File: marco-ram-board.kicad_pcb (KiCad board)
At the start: 4 copper layers, 160 x 100 mm, 185 parts, among them J201 PRG_USB, J202 MCU_RST, J203 MCU_BOOT0, J204 FT_TXD, J205 FT_RXD, J206 CONN_JTAG, J301 CONN_MCU_SERIAL, J302 CONN_EXT, J501 MCU_USB, J502 SD_Card, J503 CONN_DISP, J504 RJ45_Amphenol_RJMG1BD3B8K1ANR, J601 CONN_JACK_12V, J602 CONN_SCREW_12V, Q201 MMBT3906, Q601 DMP3037LSS, SW301 SW_RST, SW302 SW_BOOT0, SW501 BTN0, SW502 BTN1, SW503 BTN2, SW504 BTN3, SW601 PWR_SW, U201 FT2232HL, U301 STM32F765IITx, U401 IS42S86400D, U402 IS42S86400D, U403 IS42S86400D, U404 IS42S86400D, U405 IS42S86400D, U406 IS42S86400D, U407 IS42S86400D, U408 IS42S86400D, U501 KSZ8081RNA, U601 LM2576S-3.3, Y201 12MHz, Y301 25MHz

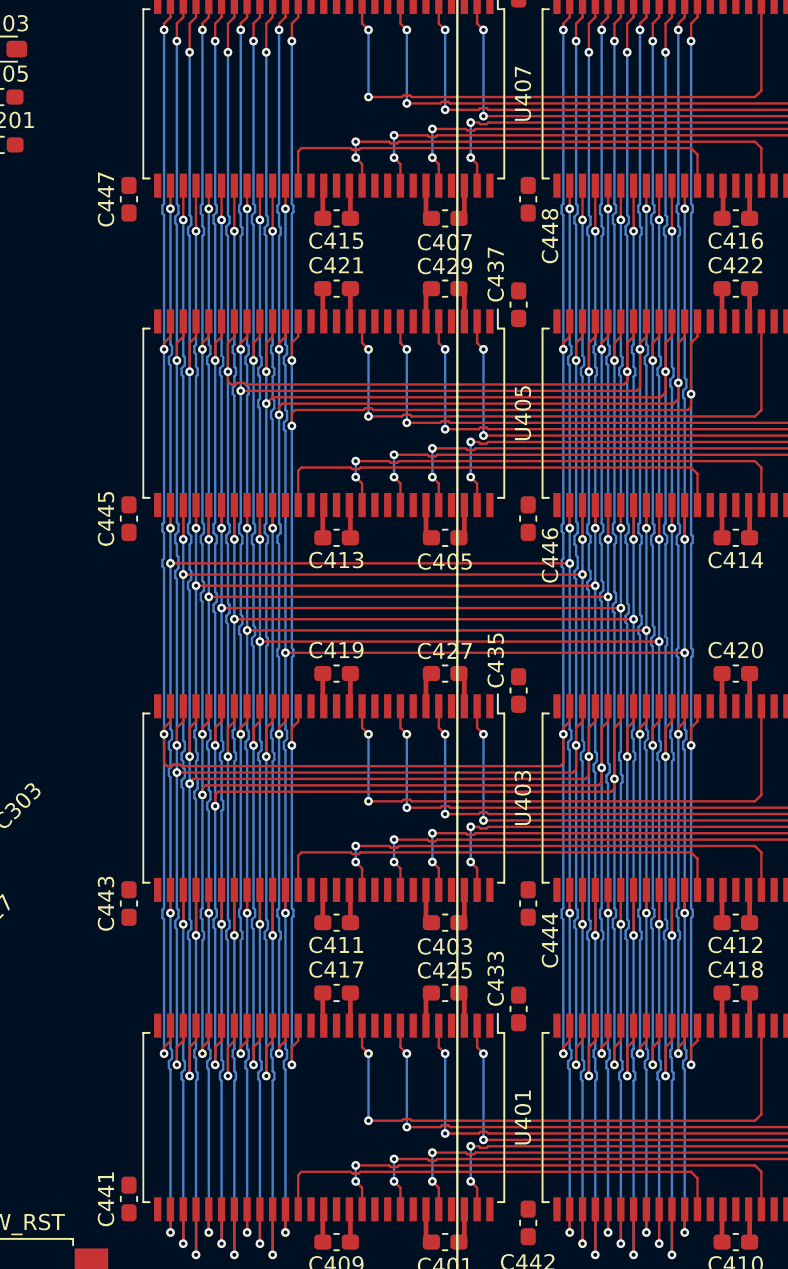
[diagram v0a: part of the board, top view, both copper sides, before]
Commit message: Bring out all SDRAM BUS elements from the SDRAM section from the closest point to the MCU
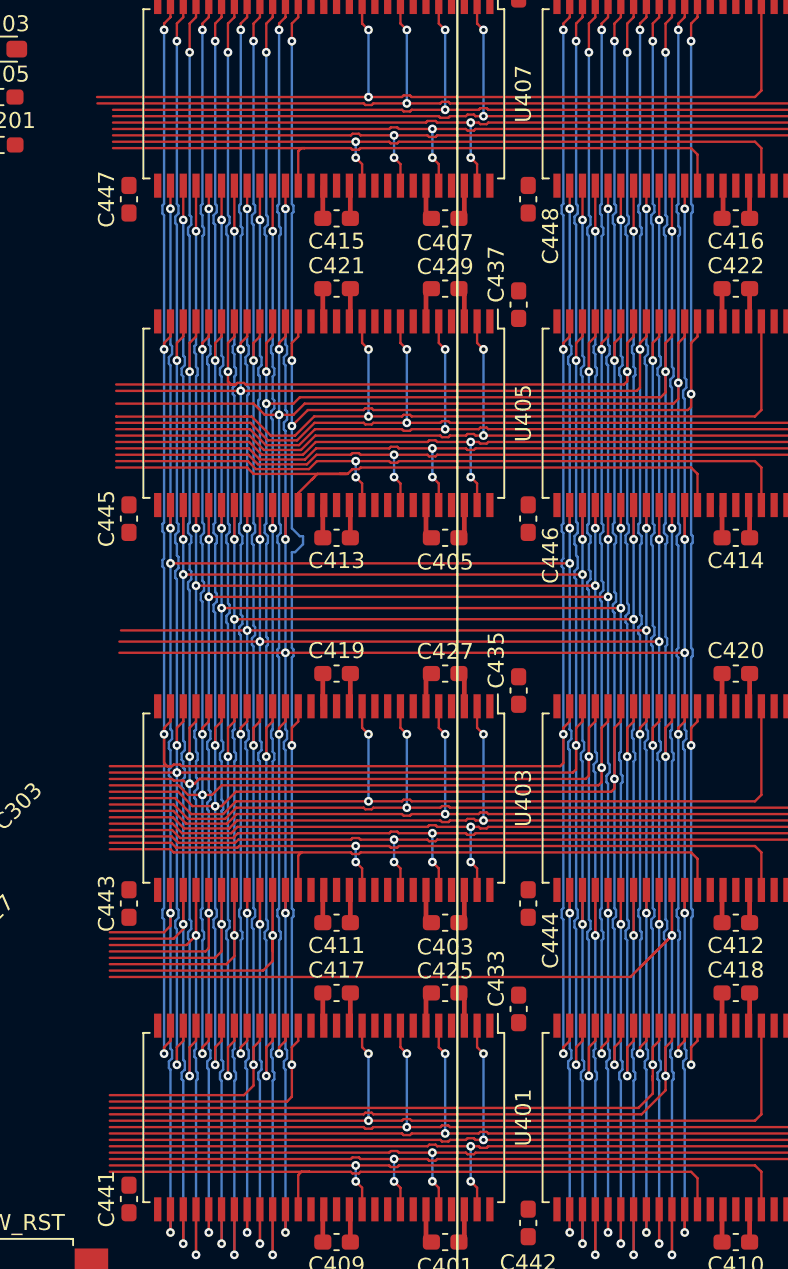
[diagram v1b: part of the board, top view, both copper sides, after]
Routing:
- net /mcu/SDRAM.CKE1: track 74.6 -> 113.7 mm
- net /mcu/SDRAM.~{CS1}: track 75.2 -> 111.7 mm
- net /mcu/SDRAM.~{RAS}: track 182.5 -> 218.9 mm
- net /mcu/SDRAM.D16: track 38.8 -> 62.9 mm
- net /mcu/SDRAM.D8: track 38.8 -> 62.7 mm
- net /mcu/SDRAM.D24: track 38.8 -> 62.4 mm
- net /mcu/SDRAM.D0: track 38.8 -> 62.2 mm
- net /mcu/SDRAM.D23: track 33.3 -> 56.4 mm
- net /mcu/SDRAM.D15: track 33.3 -> 56.3 mm
- net /mcu/SDRAM.D31: track 33.3 -> 56.0 mm
- net /mcu/SDRAM.D7: track 33.3 -> 55.8 mm
- net /mcu/SDRAM.D17: track 38.1 -> 59.8 mm
- net /mcu/SDRAM.D9: track 38.1 -> 59.6 mm
- net /mcu/SDRAM.D25: track 38.1 -> 59.2 mm
- net /mcu/SDRAM.D1: track 38.1 -> 59.0 mm
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
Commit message: Route SDRAM. Whew!
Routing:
- net /mcu/SDRAM.D26: track 56.0 -> 137.8 mm, vias 2 -> 4
- net /mcu/SDRAM.D27: track 52.7 -> 133.7 mm, vias 2 -> 4
- net /mcu/SDRAM.D25: track 59.2 -> 135.9 mm, vias 2 -> 4
- net /mcu/SDRAM.D24: track 62.4 -> 138.6 mm, vias 2 -> 4
- net /mcu/SDRAM.~{BL0}: track 41.4 -> 114.7 mm, vias 0 -> 2
- net /mcu/SDRAM.~{BL3}: track 41.9 -> 109.6 mm, vias 0 -> 2
- net /mcu/SDRAM.D28: track 46.3 -> 113.4 mm, vias 2 -> 4
- net /mcu/SDRAM.D29: track 49.6 -> 116.3 mm, vias 2 -> 4
- net /mcu/SDRAM.D7: track 55.8 -> 120.1 mm, vias 2 -> 4
- net /mcu/SDRAM.D6: track 52.6 -> 115.5 mm, vias 2 -> 4
- net /mcu/SDRAM.D5: track 49.4 -> 111.9 mm, vias 2 -> 4
- net /mcu/SDRAM.D4: track 46.1 -> 108.2 mm, vias 2 -> 4
- net /mcu/SDRAM.D30: track 52.8 -> 113.4 mm
- net /mcu/SDRAM.~{BL1}: track 43.8 -> 104.3 mm, vias 0 -> 2
- net /mcu/SDRAM.D31: track 56.0 -> 115.7 mm
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
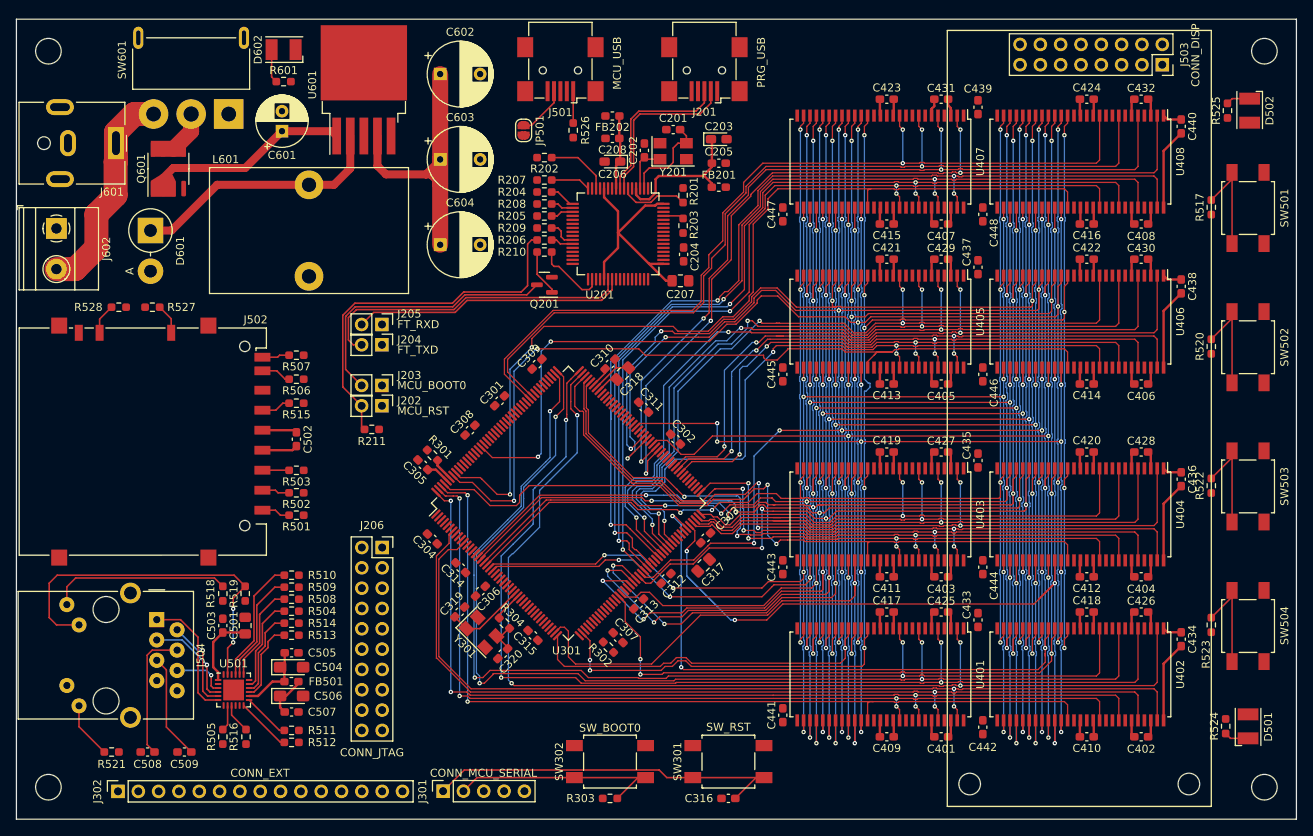
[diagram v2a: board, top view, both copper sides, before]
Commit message: SDRAM routing cleanup
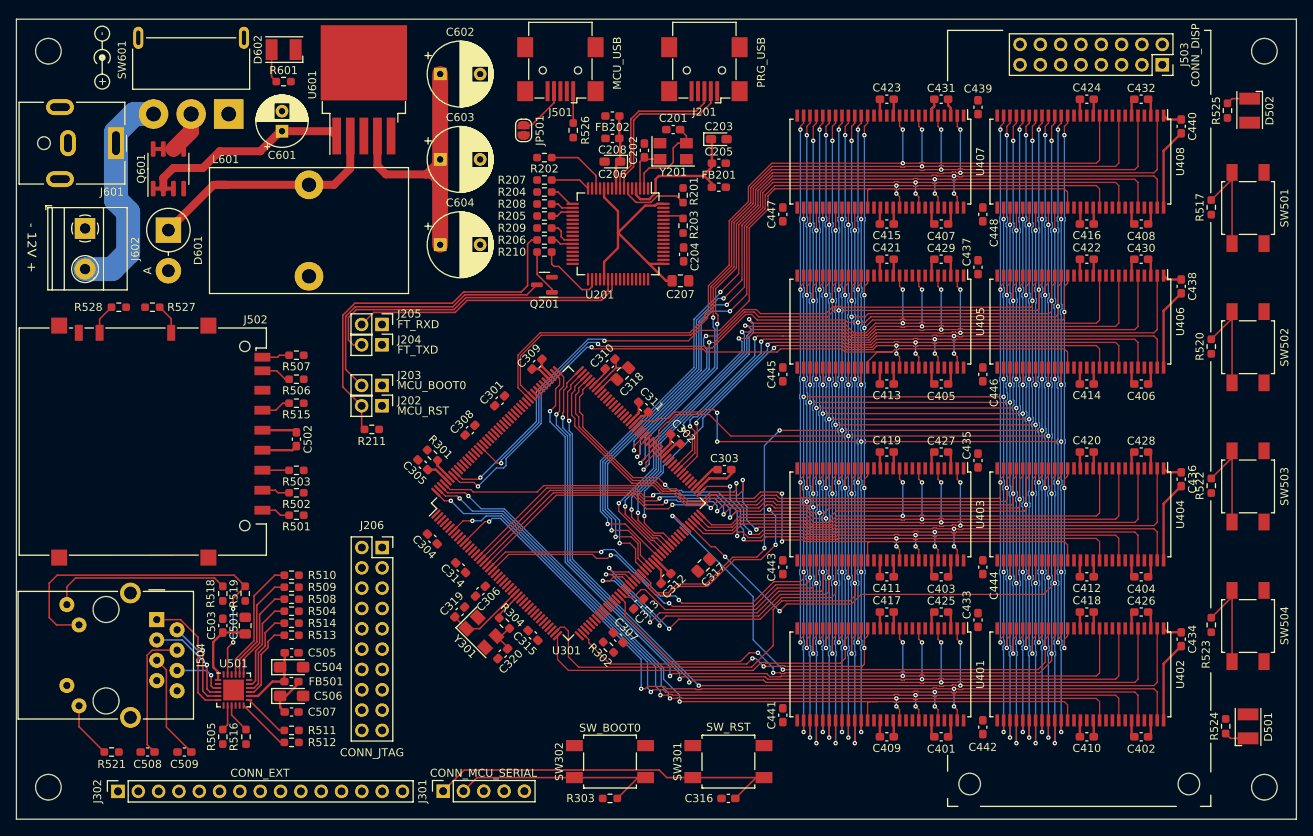
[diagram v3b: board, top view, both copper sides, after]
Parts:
- added REF**: Symbol_Barrel_Polarity, Symbol:Symbol_Barrel_Polarity, F.Cu at (80.8, 44.8)
- moved C303 8.85 mm to (158.5, 96.3), turned to 0 degrees
- moved J602 3.58 mm to (78.6, 66.2)
- moved D601 2.24 mm to (89.0, 66.4)
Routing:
- net /mcu/SDRAM.D26: track 137.8 -> 113.6 mm
- net /mcu/SDRAM.D27: track 133.7 -> 110.7 mm
- net /mcu/SDRAM.D24: track 138.6 -> 118.3 mm
- net /mcu/SDRAM.D25: track 135.9 -> 116.3 mm
- net GND: track 117.9 -> 134.3 mm
- net VDD: track 131.7 -> 146.1 mm
- net /mcu/SDRAM.CKE1: track 140.1 -> 126.1 mm
- net /mcu/SDRAM.~{BL3}: track 109.6 -> 96.3 mm
- net /mcu/SDRAM.D28: track 113.4 -> 100.5 mm
- net /mcu/SDRAM.D29: track 116.3 -> 104.1 mm
- net /mcu/SDRAM.~{BL1}: track 104.3 -> 94.6 mm
- net /mcu/SDRAM.~{BL0}: track 114.7 -> 105.4 mm
- net /mcu/SDRAM.D31: track 115.7 -> 107.0 mm, vias 2 -> 4
- net /mcu/SDRAM.D30: track 113.4 -> 104.8 mm, vias 2 -> 4
- net /mcu/SDRAM.BA0: track 219.6 -> 211.5 mm
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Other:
- board text added: "+"
- board text added: "-"
- board text added: "- 12V +"

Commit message: MCU USB
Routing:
- net /mcu-if/USB.DM: track 0.00 -> 48.9 mm, vias 0 -> 2
- net /mcu-if/USB.ID: track 0.00 -> 48.4 mm, vias 0 -> 2
- net /mcu-if/USB.DP: track 0.00 -> 47.8 mm, vias 0 -> 2
- net /mcu-if/USB.VBUS: track 0.00 -> 44.7 mm, vias 0 -> 2
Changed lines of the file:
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@@
   (segment (start 126.344974 75.15) (end 143.144975 75.15) (width 0.2) (layer "F.Cu") (net 34))
   (segment (start 139.6 49) (end 139.6 52.975) (width 0.2) (layer "F.Cu") (net 57))
+  (segment (start 137.4 53.8) (end 138.35 52.85) (width 0.2) (layer "F.Cu") (net 58))
+  (segment (start 138.35 52.85) (end 138.35 50.95) (width 0.2) (layer "F.Cu") (net 58))
+  (segment (start 138.8 50.5) (end 138.8 49) (width 0.2) (layer "F.Cu") (net 58))
+  (segment (start 138.35 50.95) (end 138.8 50.5) (width 0.2) (layer "F.Cu") (net 58))
+  (segment (start 142.7 88.668272) (end 142.7 89.2) (width 0.2) (layer "F.Cu") (net 58))
+  (segment (start 143.896714 87.471558) (end 142.7 88.668272) (width 0.2) (layer "F.Cu") (net 58))
+  (segment (start 142.7 89.2) (end 142.3 89.6) (width 0.2) (layer "F.Cu") (net 58))
+  (via (at 137.4 53.8) (size 0.55) (drill 0.25) (layers "F.Cu" "B.Cu") (net 58))
+  (via (at 142.3 89.6) (size 0.55) (drill 0.25) (layers "F.Cu" "B.Cu") (net 58))
+  (segment (start 145.75 85.45) (end 142.7 88.5) (width 0.2) (layer "B.Cu") (net 58))
+  (segment (start 138.35 54.75) (end 138.35 69.255026) (width 0.2) (layer "B.Cu") (net 58))
+  (segment (start 138.35 69.255026) (end 145.75 76.655026) (width 0.2) (layer "B.Cu") (net 58))
+  (segment (start 142.7 89.2) (end 142.3 89.6) (width 0.2) (layer "B.Cu") (net 58))
+  (segment (start 145.75 76.655026) (end 145.75 85.45) (width 0.2) (layer "B.Cu") (net 58))
+  (segment (start 142.7 88.5) (end 142.7 89.2) (width 0.2) (layer "B.Cu") (net 58))
+  (segment (start 137.4 53.8) (end 138.35 54.75) (width 0.2) (layer "B.Cu") (net 58))
+  (segment (start 143.543161 87.118004) (end 141.9 88.761165) (width 0.2) (layer "F.Cu") (net 59))
+  (segment (start 141.9 88.761165) (end 141.9 88.8) (width 0.2) (layer "F.Cu") (net 59))
+  (segment (start 136.6 53.4) (end 138 52) (width 0.2) (layer "F.Cu") (net 59))
+  (segment (start 138 52) (end 138 49) (width 0.2) (layer "F.Cu") (net 59))
+  (via (at 141.9 88.8) (size 0.55) (drill 0.25) (layers "F.Cu" "B.Cu") (net 59))
+  (via (at 136.6 53.4) (size 0.55) (drill 0.25) (layers "F.Cu" "B.Cu") (net 59))
+  (segment (start 145.4 85.3) (end 145.4 76.8) (width 0.2) (layer "B.Cu") (net 59))
+  (segment (start 136.6 53.9) (end 136.6 53.4) (width 0.2) (layer "B.Cu") (net 59))
+  (segment (start 141.9 88.8) (end 145.4 85.3) (width 0.2) (layer "B.Cu") (net 59))
+  (segment (start 139.2 70.6) (end 138 69.4) (width 0.2) (layer "B.Cu") (net 59))
+  (segment (start 145.4 76.8) (end 139.2 70.6) (width 0.2) (layer "B.Cu") (net 59))
+  (segment (start 138 69.4) (end 138 55.3) (width 0.2) (layer "B.Cu") (net 59))
+  (segment (start 138 55.3) (end 136.6 53.9) (width 0.2) (layer "B.Cu") (net 59))
   (segment (start 137.2 50.45) (end 134.4 53.25) (width 0.2) (layer "F.Cu") (net 60))
   (segment (start 137.2 49) (end 137.2 50.45) (width 0.2) (layer "F.Cu") (net 60))
@@
   (segment (start 93.756 121.407) (end 90.086 121.407) (width 0.2) (layer "B.Cu") (net 80))
   (segment (start 94.349 122) (end 93.756 121.407) (width 0.2) (layer "B.Cu") (net 80))
+  (segment (start 143.3 88.775379) (end 143.3 89.5) (width 0.2) (layer "F.Cu") (net 82))
+  (segment (start 143.3 89.8) (end 142.7 90.4) (width 0.2) (layer "F.Cu") (net 82))
+  (segment (start 135.9 54.5) (end 133.45 54.5) (width 0.2) (layer "F.Cu") (net 82))
+  (segment (start 143.3 89.5) (end 143.3 89.8) (width 0.2) (layer "F.Cu") (net 82))
+  (segment (start 144.250268 87.825111) (end 143.3 88.775379) (width 0.2) (layer "F.Cu") (net 82))
+  (segment (start 133.45 54.5) (end 133.4 54.55) (width 0.2) (layer "F.Cu") (net 82))
+  (via (at 142.7 90.4) (size 0.55) (drill 0.25) (layers "F.Cu" "B.Cu") (net 82))
+  (via (at 135.9 54.5) (size 0.55) (drill 0.25) (layers "F.Cu" "B.Cu") (net 82))
+  (segment (start 142.305026 87.9) (end 145.05 85.155026) (width 0.2) (layer "B.Cu") (net 82))
+  (segment (start 137.3 55.8) (end 136 54.5) (width 0.2) (layer "B.Cu") (net 82))
+  (segment (start 142.3 87.9) (end 142.305026 87.9) (width 0.2) (layer "B.Cu") (net 82))
+  (segment (start 141.6 90) (end 141.2 89.6) (width 0.2) (layer "B.Cu") (net 82))
+  (segment (start 137.65 56.15) (end 137.3 55.8) (width 0.2) (layer "B.Cu") (net 82))
+  (segment (start 137.65 64.9) (end 137.65 56.15) (width 0.2) (layer "B.Cu") (net 82))
+  (segment (start 141.6 88.1) (end 141.8 87.9) (width 0.2) (layer "B.Cu") (net 82))
+  (segment (start 145.05 84) (end 145.05 77.3) (width 0.2) (layer "B.Cu") (net 82))
+  (segment (start 144.402513 76.297487) (end 137.65 69.544974) (width 0.2) (layer "B.Cu") (net 82))
+  (segment (start 141.2 88.5) (end 141.6 88.1) (width 0.2) (layer "B.Cu") (net 82))
+  (segment (start 145.05 77.3) (end 145.05 76.944974) (width 0.2) (layer "B.Cu") (net 82))
+  (segment (start 136 54.5) (end 135.9 54.5) (width 0.2) (layer "B.Cu") (net 82))
+  (segment (start 141.2 88.7) (end 141.2 88.5) (width 0.2) (layer "B.Cu") (net 82))
+  (segment (start 141.2 89.6) (end 141.2 88.7) (width 0.2) (layer "B.Cu") (net 82))
+  (segment (start 137.65 69.544974) (end 137.65 64.9) (width 0.2) (layer "B.Cu") (net 82))
+  (segment (start 142 90.4) (end 141.6 90) (width 0.2) (layer "B.Cu") (net 82))
+  (segment (start 141.8 87.9) (end 142.3 87.9) (width 0.2) (layer "B.Cu") (net 82))
+  (segment (start 145.05 85.155026) (end 145.05 84) (width 0.2) (layer "B.Cu") (net 82))
+  (segment (start 145.05 76.944974) (end 144.402513 76.297487) (width 0.2) (layer "B.Cu") (net 82))
+  (segment (start 142.7 90.4) (end 142 90.4) (width 0.2) (layer "B.Cu") (net 82))
   (segment (start 136.9375 74.15) (end 136.9375 73.7375) (width 0.2) (layer "F.Cu") (net 83))
   (segment (start 136.9375 73.7375) (end 135.0875 71.8875) (width 0.2) (layer "F.Cu") (net 83))
@@
   (segment (start 219.36 114.802857) (end 221.96 112.202857) (width 0.2) (layer "F.Cu") (net 121))
   (segment (start 221.96 111.402857) (end 221.96 120.302857) (width 0.2) (layer "F.Cu") (net 121))
+  (segment (start 143.7 89.082485) (end 143.7 90.6) (width 0.2) (layer "F.Cu") (net 122))
+  (segment (start 143.7 90.6) (end 143.1 91.2) (width 0.2) (layer "F.Cu") (net 122))
+  (segment (start 144.603821 88.178664) (end 143.7 89.082485) (width 0.2) (layer "F.Cu") (net 122))
+  (segment (start 139.6 56.3) (end 139.6 54.8) (width 0.2) (layer "F.Cu") (net 122))
+  (via (at 139.6 56.3) (size 0.55) (drill 0.25) (layers "F.Cu" "B.Cu") (net 122))
+  (via (at 143.1 91.2) (size 0.55) (drill 0.25) (layers "F.Cu" "B.Cu") (net 122))
+  (segment (start 143.5 88.194974) (end 143.5 90.8) (width 0.2) (layer "B.Cu") (net 122))
+  (segment (start 138.7 57.2) (end 138.7 69.110052) (width 0.2) (layer "B.Cu") (net 122))
+  (segment (start 138.7 69.110052) (end 146.089948 76.5) (width 0.2) (layer "B.Cu") (net 122))
+  (segment (start 143.5 90.8) (end 143.1 91.2) (width 0.2) (layer "B.Cu") (net 122))
+  (segment (start 146.1 76.5) (end 146.1 85.594974) (width 0.2) (layer "B.Cu") (net 122))
+  (segment (start 146.1 85.594974) (end 143.5 88.194974) (width 0.2) (layer "B.Cu") (net 122))
+  (segment (start 146.089948 76.5) (end 146.1 76.5) (width 0.2) (layer "B.Cu") (net 122))
+  (segment (start 139.6 56.3) (end 138.7 57.2) (width 0.2) (layer "B.Cu") (net 122))
   (segment (start 151.1 124.1) (end 182.1 124.1) (width 0.15) (layer "F.Cu") (net 155))
   (segment (start 124.557344 103.982501) (end 125.839845 102.7) (width 0.15) (layer "F.Cu") (net 155))
